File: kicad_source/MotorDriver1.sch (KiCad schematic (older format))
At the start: 19 parts, among them P5 CONN_01X04, P6 CONN_01X05, U2 TMC5130A-TA

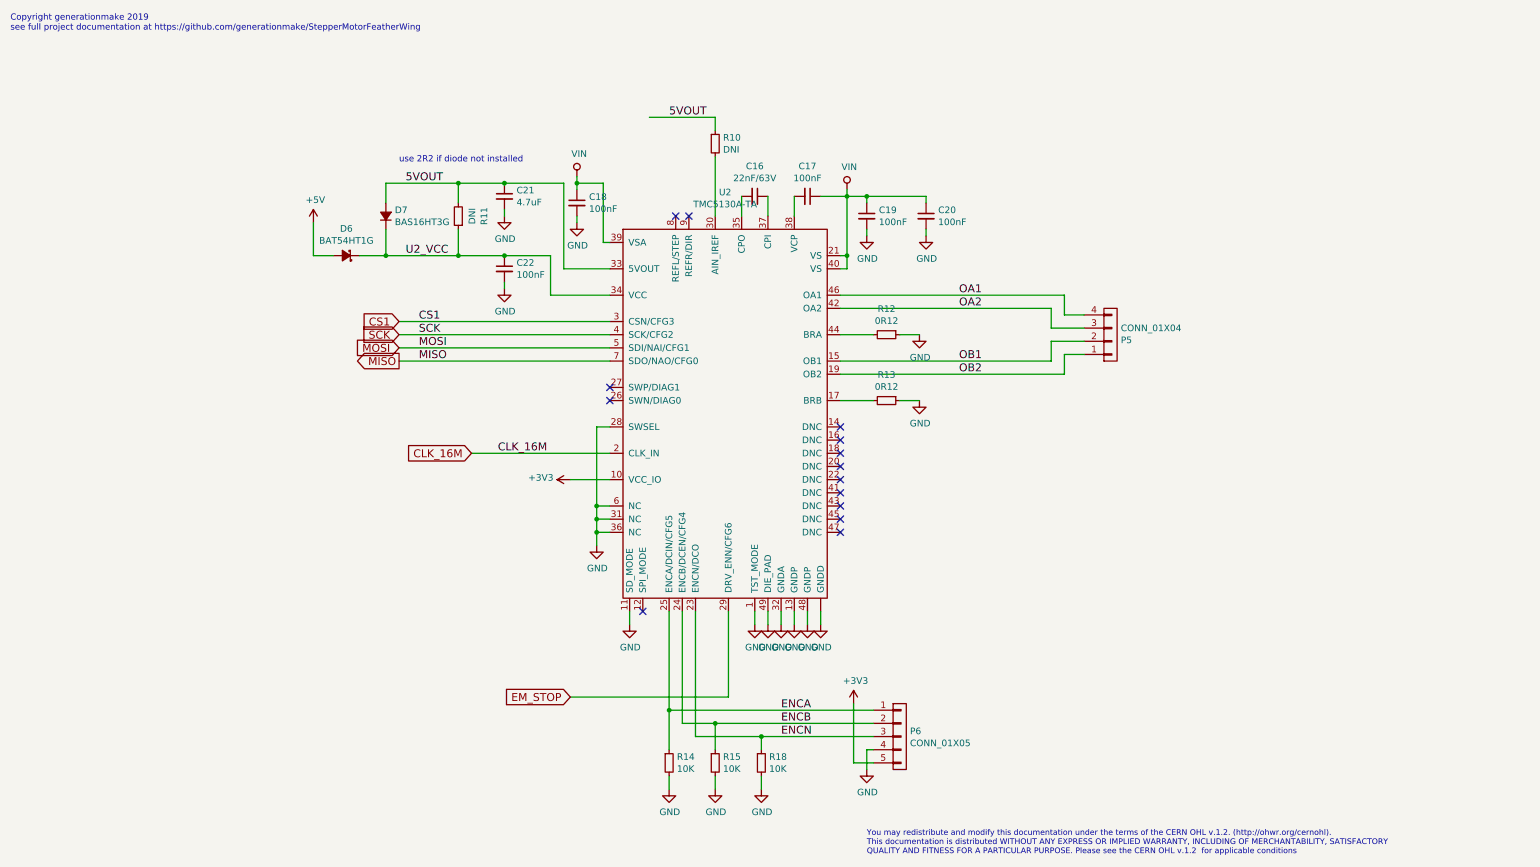
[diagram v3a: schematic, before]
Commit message: added leds and decoupling capacitors
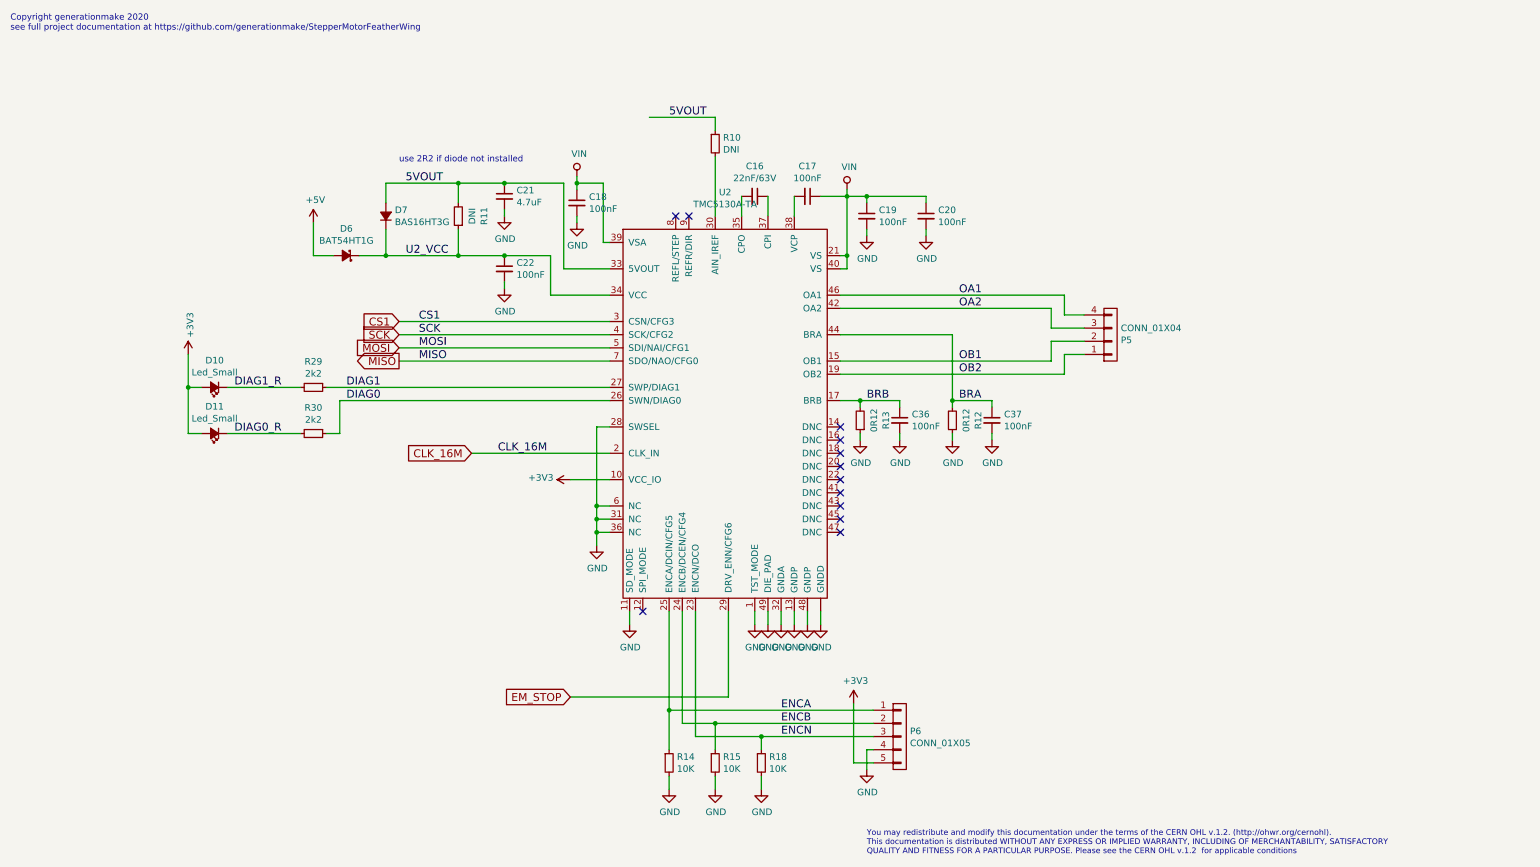
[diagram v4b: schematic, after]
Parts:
- added C36, C37: 100nF, capacitors:C_0603, symbol devices:C_0603
- added D10, D11: Led_Small, LEDs:LED_0603, symbol devices:Led_Small
- added R29, R30: 2k2, resistors:R_0603, symbol devices:R_0603
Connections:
- net +3V3: now also D10.2 (A), D11.2 (A)
- net GND: now also C36.2, C37.2
- net BRB: now reaches R13.2, U2.17 (BRB)
- net BRB: now also C36.1
- net DIAG0: now reaches U2.26 (SWN/DIAG0)
- net DIAG0: now also R30.1
- net DIAG1: now reaches U2.27 (SWP/DIAG1)
- net DIAG1: now also R29.1
- net BRA: now reaches R12.2, U2.44 (BRA)
- net BRA: now also C37.1
- new net DIAG0_R: D11.1 (K), R30.2
- new net DIAG1_R: D10.1 (K), R29.2
- no-connect marks 14 -> 12
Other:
- note added: "Copyright generationmake 2020\nsee full project documentation at https://github.com/generationmake/StepperMotorFeatherWing"
- note removed: "Copyright generationmake 2019\nsee full project documentation at https://github.com/generationmake/StepperMotorFeatherWing"
- moved on the sheet: R12, R13
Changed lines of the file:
@@
 Sheet 4 6
 Title "HighPowerMotorFeatherWing"
-Date "2019-12-31"
-Rev "1.0"
+Date "2020-07-04"
+Rev "1.1"
 Comp "generationmake"
 Comment1 ""
@@
 $EndDescr
 Text Notes 500  650  0    47   ~ 0
-Copyright generationmake 2019\nsee full project documentation at https://github.com/generationmake/StepperMotorFeatherWing
+Copyright generationmake 2020\nsee full project documentation at https://github.com/generationmake/StepperMotorFeatherWing
 Text Notes 7000 6900 0    43   ~ 0
 You may redistribute and modify this documentation under the terms of the CERN OHL v.1.2. (http://ohwr.org/cernohl). \nThis documentation is distributed WITHOUT ANY EXPRESS OR IMPLIED WARRANTY, INCLUDING OF MERCHANTABILITY, SATISFACTORY \nQUALITY AND FITNESS FOR A PARTICULAR PURPOSE. Please see the CERN OHL v.1.2  for applicable conditions
@@
 L devices:R_0805 R12
 U 1 1 5DF3422D
-P 7150 2950
-F 0 "R12" V 6954 2950 50  0000 C CNN
-F 1 "0R12" V 7045 2950 50  0000 C CNN
-F 2 "resistors:R_0805" H 7150 2800 50  0001 C CNN
-F 3 "" H 7150 2950 50  0000 C CNN
-	1    7150 2950
-	0    1    1    0
+P 7650 3600
+F 0 "R12" V 7454 3600 50  0000 C CNN
+F 1 "0R12" V 7545 3600 50  0000 C CNN
+F 2 "resistors:R_0805" H 7650 3450 50  0001 C CNN
+F 3 "" H 7650 3600 50  0000 C CNN
+	1    7650 3600
+	-1   0    0    1
 $EndComp
 $Comp
 L devices:R_0805 R13
 U 1 1 5DED18D5
-P 7150 3450
-F 0 "R13" V 6954 3450 50  0000 C CNN
-F 1 "0R12" V 7045 3450 50  0000 C CNN
-F 2 "resistors:R_0805" H 7150 3300 50  0001 C CNN
-F 3 "" H 7150 3450 50  0000 C CNN
-	1    7150 3450
-	0    1    1    0
+P 6950 3600
+F 0 "R13" V 6754 3600 50  0000 C CNN
+F 1 "0R12" V 6845 3600 50  0000 C CNN
+F 2 "resistors:R_0805" H 6950 3450 50  0001 C CNN
+F 3 "" H 6950 3600 50  0000 C CNN
+	1    6950 3600
+	-1   0    0    1
 $EndComp
 $Comp
 L power-supply:GND #PWR049
 U 1 1 5DF3508D
-P 7400 2950
-F 0 "#PWR049" H 7400 2700 50  0001 C CNN
-F 1 "GND" H 7405 2777 50  0000 C CNN
-F 2 "" H 7400 2950 50  0000 C CNN
-F 3 "" H 7400 2950 50  0000 C CNN
-	1    7400 2950
+P 7650 3750
+F 0 "#PWR049" H 7650 3500 50  0001 C CNN
+F 1 "GND" H 7655 3577 50  0000 C CNN
+F 2 "" H 7650 3750 50  0000 C CNN
+F 3 "" H 7650 3750 50  0000 C CNN
+	1    7650 3750
 	1    0    0    -1
 $EndComp
@@
 L power-supply:GND #PWR050
 U 1 1 5DF35371
-P 7400 3450
-F 0 "#PWR050" H 7400 3200 50  0001 C CNN
-F 1 "GND" H 7405 3277 50  0000 C CNN
-F 2 "" H 7400 3450 50  0000 C CNN
-F 3 "" H 7400 3450 50  0000 C CNN
-	1    7400 3450
+P 6950 3750
+F 0 "#PWR050" H 6950 3500 50  0001 C CNN
+F 1 "GND" H 6955 3577 50  0000 C CNN
+F 2 "" H 6950 3750 50  0000 C CNN
+F 3 "" H 6950 3750 50  0000 C CNN
+	1    6950 3750
 	1    0    0    -1
 $EndComp
@@
 $EndComp
 Wire Wire Line
-	7050 2950 6800 2950
-Wire Wire Line
-	7250 3450 7400 3450
-Wire Wire Line
-	6800 3450 7050 3450
-Wire Wire Line
-	7250 2950 7400 2950
-Wire Wire Line
 	6800 3150 8400 3150
 Wire Wire Line
@@
 Wire Wire Line
 	7050 6000 6200 6000
-NoConn ~ 5050 3350
-NoConn ~ 5050 3450
 Wire Wire Line
 	3450 2850 5050 2850
@@
 Text Label 4200 3850 0    60   ~ 0
 CLK_16M
+$Comp
+L devices:R_0603 R29
+U 1 1 5F025930
+P 2800 3350
+F 0 "R29" V 2604 3350 50  0000 C CNN
+F 1 "2k2" V 2695 3350 50  0000 C CNN
+F 2 "resistors:R_0603" H 2800 3200 50  0001 C CNN
+F 3 "" H 2800 3350 50  0000 C CNN
+	1    2800 3350
+	0    1    1    0
+$EndComp
+$Comp
+L devices:Led_Small D10
+U 1 1 5F0261B0
+P 2050 3350
+F 0 "D10" H 2050 3145 50  0000 C CNN
+F 1 "Led_Small" H 2050 3236 50  0000 C CNN
+F 2 "LEDs:LED_0603" V 2050 3350 50  0001 C CNN
+F 3 "" V 2050 3350 50  0000 C CNN
+	1    2050 3350
+	-1   0    0    1
+$EndComp
+$Comp
+L devices:R_0603 R30
+U 1 1 5F032369
+P 2800 3700
+F 0 "R30" V 2604 3700 50  0000 C CNN
+F 1 "2k2" V 2695 3700 50  0000 C CNN
+F 2 "resistors:R_0603" H 2800 3550 50  0001 C CNN
+F 3 "" H 2800 3700 50  0000 C CNN
+	1    2800 3700
+	0    1    1    0
+$EndComp
+$Comp
+L devices:Led_Small D11
+U 1 1 5F032373
+P 2050 3700
+F 0 "D11" H 2050 3495 50  0000 C CNN
+F 1 "Led_Small" H 2050 3586 50  0000 C CNN
+F 2 "LEDs:LED_0603" V 2050 3700 50  0001 C CNN
+F 3 "" V 2050 3700 50  0000 C CNN
+	1    2050 3700
+	-1   0    0    1
+$EndComp
+Wire Wire Line
+	3000 3450 3000 3700
+Wire Wire Line
+	3000 3700 2900 3700
+Wire Wire Line
+	1950 3350 1850 3350
+Wire Wire Line
+	1850 3350 1850 3700
+Wire Wire Line
+	1950 3700 1850 3700
+Text Label 3050 3350 0    60   ~ 0
+DIAG1
+Text Label 3050 3450 0    60   ~ 0
+DIAG0
+$Comp
+L power-supply:+3V3 #PWR0100
+U 1 1 5F054865
+P 1850 3100
+F 0 "#PWR0100" H 1850 2950 50  0001 C CNN
+F 1 "+3V3" V 1865 3228 50  0000 L CNN
+F 2 "" H 1850 3100 50  0000 C CNN
+F 3 "" H 1850 3100 50  0000 C CNN
+	1    1850 3100
+	1    0    0    -1
+$EndComp
+Wire Wire Line
+	1850 3100 1850 3350
+Connection ~ 1850 3350
+Wire Wire Line
+	2150 3350 2700 3350
+Wire Wire Line
+	2150 3700 2700 3700
+Text Label 2200 3700 0    60   ~ 0
+DIAG0_R
+Text Label 2200 3350 0    60   ~ 0
+DIAG1_R
+Wire Wire Line
+	2900 3350 5050 3350
+Wire Wire Line
+	3000 3450 5050 3450
+$Comp
+L devices:C_0603 C36
+U 1 1 5F0A7325
+P 7250 3600
+F 0 "C36" H 7342 3646 50  0000 L CNN
+F 1 "100nF" H 7342 3555 50  0000 L CNN
+F 2 "capacitors:C_0603" H 7250 3450 50  0001 C CNN
+F 3 "" H 7250 3600 50  0000 C CNN
+	1    7250 3600
+	1    0    0    -1
+$EndComp
+$Comp
+L devices:C_0603 C37
+U 1 1 5F0AD383
+P 7950 3600
+F 0 "C37" H 8042 3646 50  0000 L CNN
+F 1 "100nF" H 8042 3555 50  0000 L CNN
+F 2 "capacitors:C_0603" H 7950 3450 50  0001 C CNN
+F 3 "" H 7950 3600 50  0000 C CNN
+	1    7950 3600
+	1    0    0    -1
+$EndComp
+$Comp
+L power-supply:GND #PWR0101
+U 1 1 5F0AF0D5
+P 7250 3750
+F 0 "#PWR0101" H 7250 3500 50  0001 C CNN
+F 1 "GND" H 7255 3577 50  0000 C CNN
+F 2 "" H 7250 3750 50  0000 C CNN
+F 3 "" H 7250 3750 50  0000 C CNN
+	1    7250 3750
+	1    0    0    -1
+$EndComp
+$Comp
+L power-supply:GND #PWR0102
+U 1 1 5F0AF2A7
+P 7950 3750
+F 0 "#PWR0102" H 7950 3500 50  0001 C CNN
+F 1 "GND" H 7955 3577 50  0000 C CNN
+F 2 "" H 7950 3750 50  0000 C CNN
+F 3 "" H 7950 3750 50  0000 C CNN
+	1    7950 3750
+	1    0    0    -1
+$EndComp
+Wire Wire Line
+	6800 3450 6950 3450
+Wire Wire Line
+	7250 3450 7250 3500
+Wire Wire Line
+	7650 2950 7650 3450
+Wire Wire Line
+	6800 2950 7650 2950
+Wire Wire Line
+	7650 3450 7950 3450
+Wire Wire Line
+	7950 3450 7950 3500
+Connection ~ 7650 3450
+Wire Wire Line
+	7650 3450 7650 3500
+Wire Wire Line
+	7950 3700 7950 3750
+Wire Wire Line
+	7650 3700 7650 3750
+Wire Wire Line
+	7250 3700 7250 3750
+Wire Wire Line
+	6950 3750 6950 3700
+Wire Wire Line
+	6950 3500 6950 3450
+Connection ~ 6950 3450
+Wire Wire Line
+	6950 3450 7250 3450
+Text Label 7700 3450 0    60   ~ 0
+BRA
+Text Label 7000 3450 0    60   ~ 0
+BRB
 $EndSCHEMATC

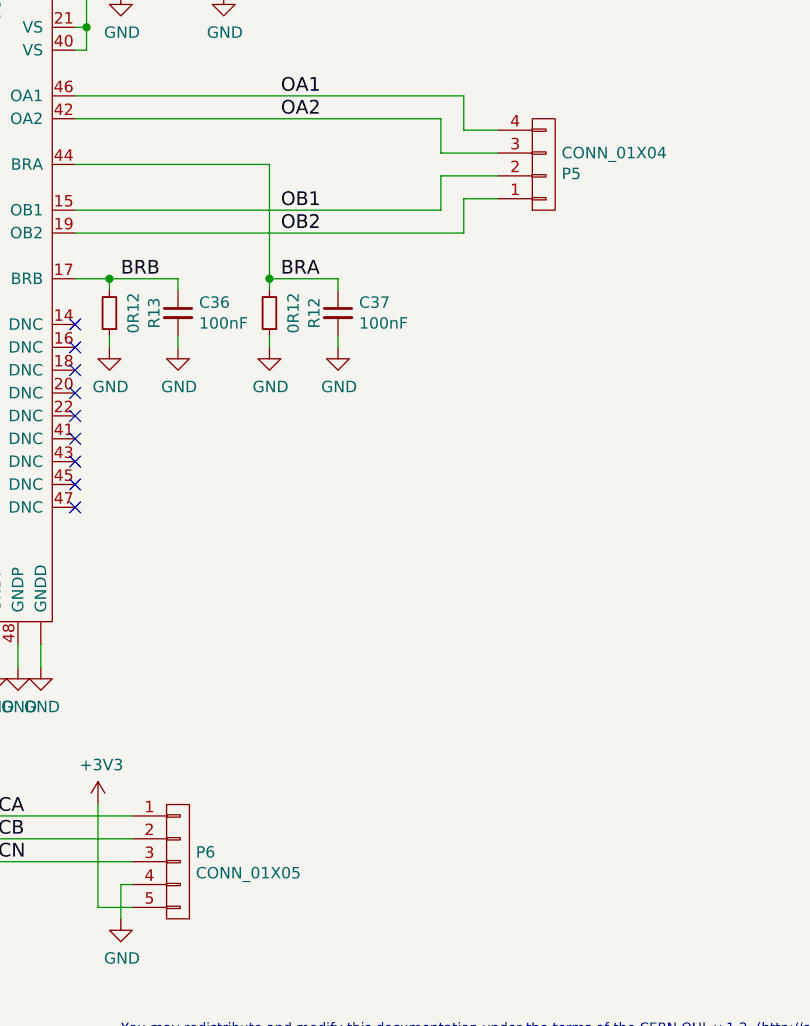
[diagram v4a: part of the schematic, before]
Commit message: changed type of encoder connector
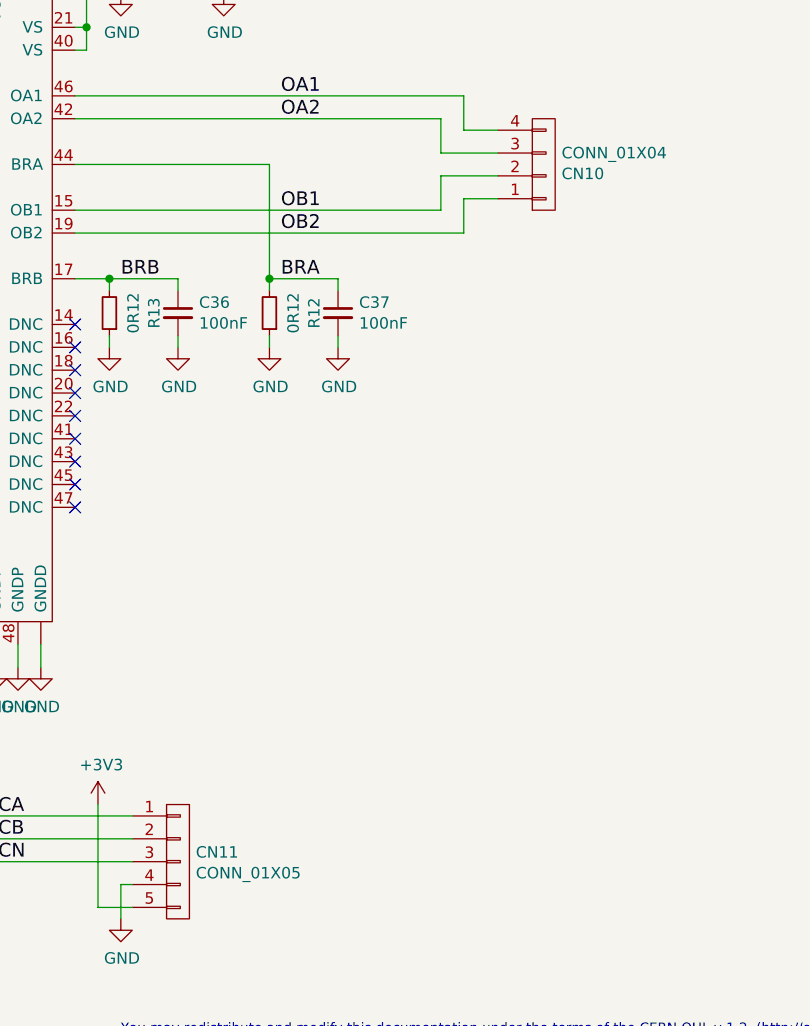
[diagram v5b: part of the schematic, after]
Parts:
- CN11: renamed from P6; footprint CON_wuerth:WR-TBL_691322310005 -> connectors_JST_PH:Connectors_JST_S5B-PH-SM4-TB
- renumbered P5 to CN10
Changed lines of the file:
@@
 $EndComp
 $Comp
-L mechanical-connectors:CONN_01X04 P5
+L mechanical-connectors:CONN_01X04 CN10
 U 1 1 5DF357FF
 P 8850 2950
-F 0 "P5" H 8928 2991 50  0000 L CNN
+F 0 "CN10" H 8928 2991 50  0000 L CNN
 F 1 "CONN_01X04" H 8928 2900 50  0000 L CNN
 F 2 "CON_wuerth:WR-TBL_691322310004" H 8850 2950 50  0001 C CNN
@@
 NoConn ~ 5300 5050
 $Comp
-L mechanical-connectors:CONN_01X05 P6
+L mechanical-connectors:CONN_01X05 CN11
 U 1 1 5DED18E4
 P 7250 6000
-F 0 "P6" H 7328 6041 50  0000 L CNN
+F 0 "CN11" H 7328 6041 50  0000 L CNN
 F 1 "CONN_01X05" H 7328 5950 50  0000 L CNN
-F 2 "CON_wuerth:WR-TBL_691322310005" H 7250 6000 50  0001 C CNN
+F 2 "connectors_JST_PH:Connectors_JST_S5B-PH-SM4-TB" H 7250 6000 50  0001 C CNN
 F 3 "" H 7250 6000 50  0000 C CNN
 	1    7250 6000

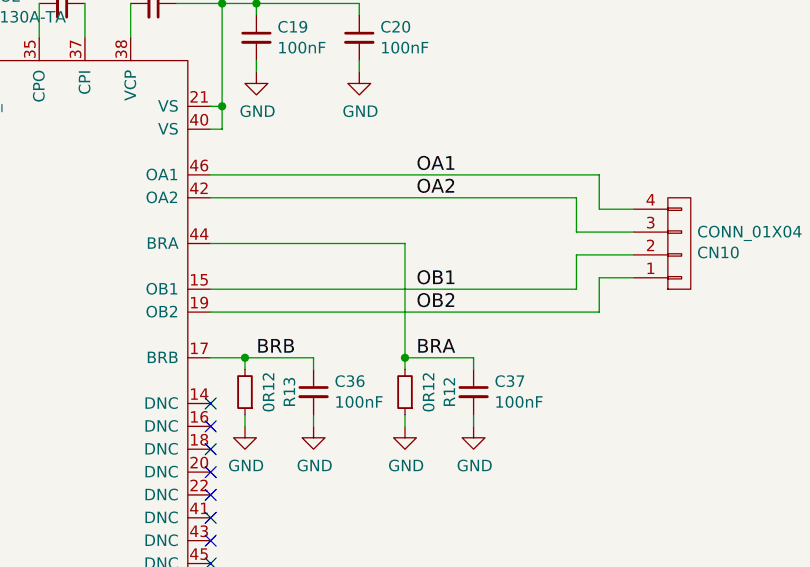
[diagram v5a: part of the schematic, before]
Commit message: updated layout
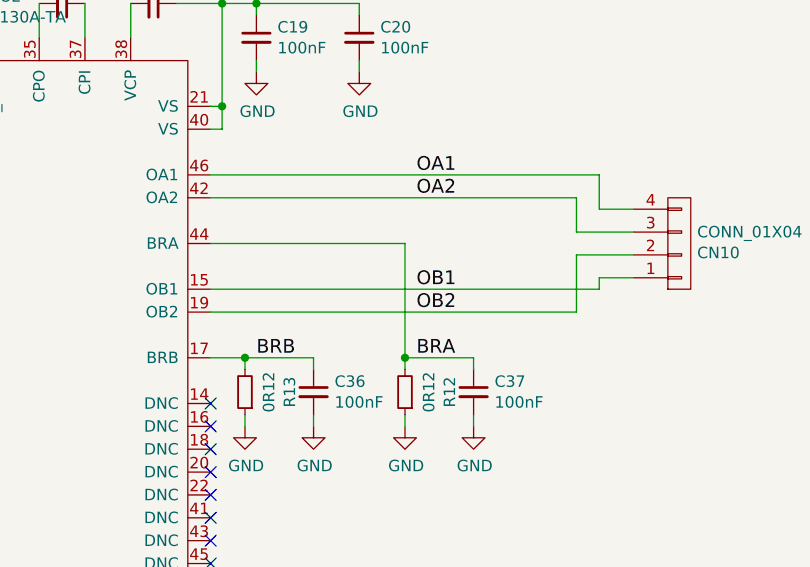
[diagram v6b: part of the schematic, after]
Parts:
- CN11: footprint connectors_JST_PH:Connectors_JST_S5B-PH-SM4-TB -> connectors_JST_SH:Connectors_JST_BM05B-SRSS-TB
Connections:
- net OB1: now also CN10.1 (P1); no longer CN10.2 (P2)
- net OB2: now also CN10.2 (P2); no longer CN10.1 (P1)
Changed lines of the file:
@@
 $EndComp
-Wire Wire Line
-	6800 3150 8400 3150
-Wire Wire Line
-	8400 3150 8400 3000
 Wire Wire Line
 	8400 3000 8650 3000
 Wire Wire Line
-	6800 3250 8500 3250
-Wire Wire Line
-	8500 3250 8500 3100
+	6800 3250 8400 3250
 Wire Wire Line
 	8500 3100 8650 3100
@@
 F 0 "CN11" H 7328 6041 50  0000 L CNN
 F 1 "CONN_01X05" H 7328 5950 50  0000 L CNN
-F 2 "connectors_JST_PH:Connectors_JST_S5B-PH-SM4-TB" H 7250 6000 50  0001 C CNN
+F 2 "connectors_JST_SH:Connectors_JST_BM05B-SRSS-TB" H 7250 6000 50  0001 C CNN
 F 3 "" H 7250 6000 50  0000 C CNN
 	1    7250 6000
@@
 Text Label 7000 3450 0    60   ~ 0
 BRB
+Wire Wire Line
+	8500 3150 8500 3100
+Wire Wire Line
+	6800 3150 8500 3150
+Wire Wire Line
+	8400 3000 8400 3250
 $EndSCHEMATC
